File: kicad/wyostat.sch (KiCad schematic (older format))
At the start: 75 parts, among them J1 24 V AC IN, J13 USB_microAB, J16 5V_SEL, J2 OUT1, J3 OUT2, J4 OUT3, J5 I2C_ext1, Q1 BT136-600, Q2 BT136-600, Q3 BT136-600, U1 MOC3063M, U2 MOC3063M, U3 MOC3063M, U4 Wemos-Lolin, U5 MAX17502FATB+T

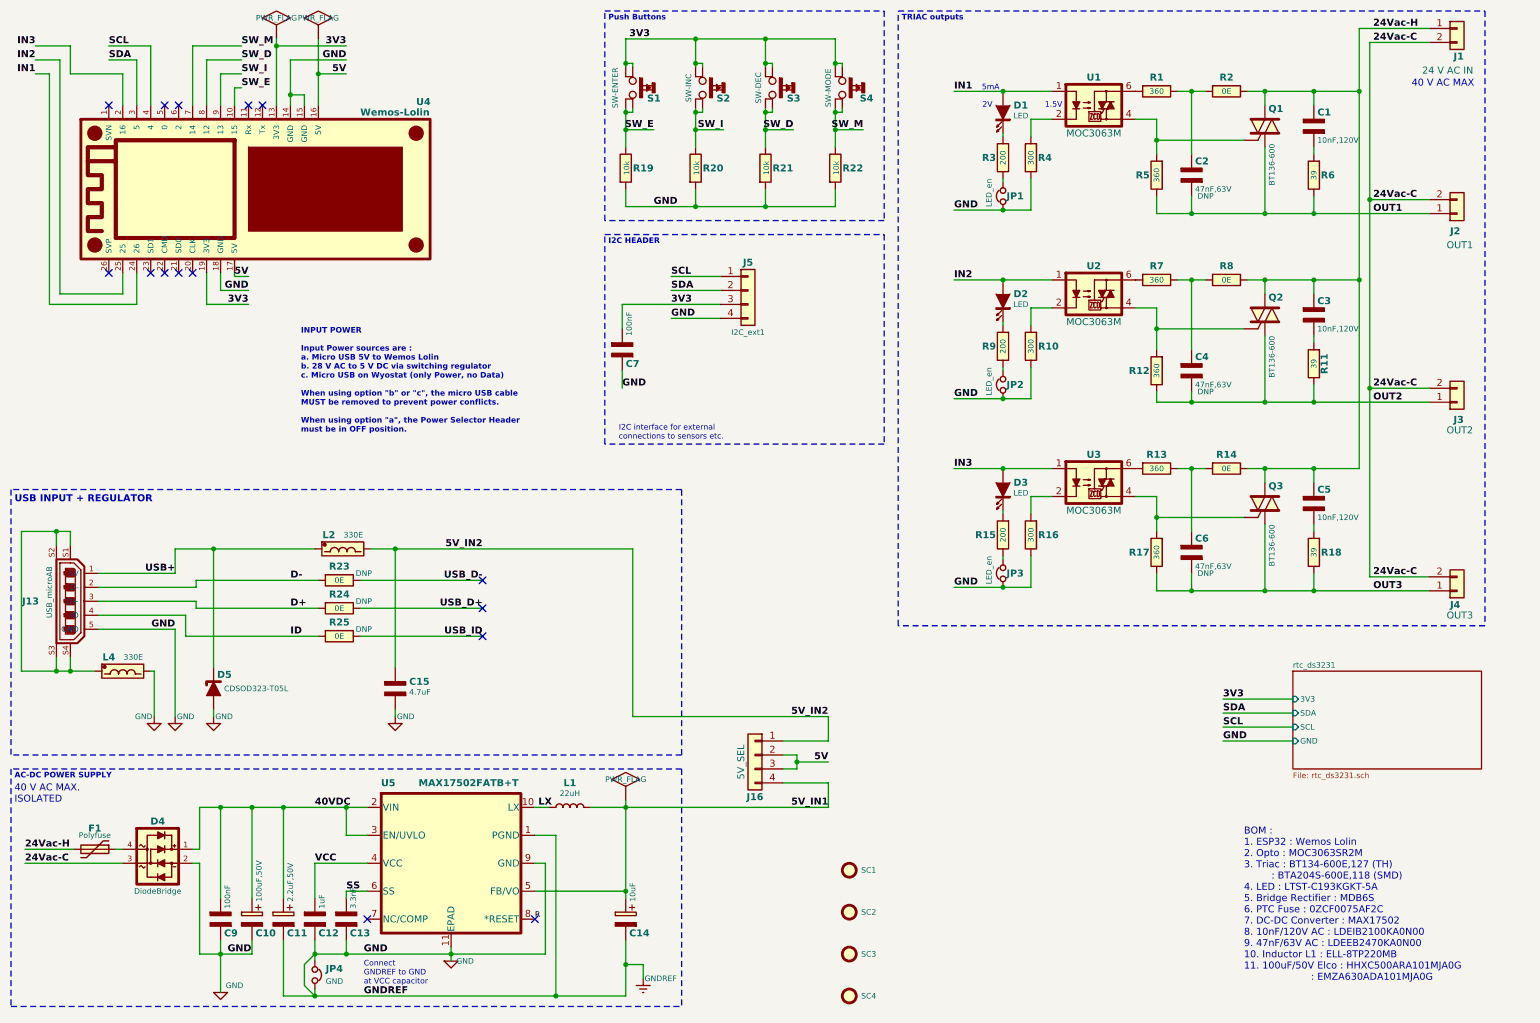
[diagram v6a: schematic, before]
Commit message: adding pads for spring contacts
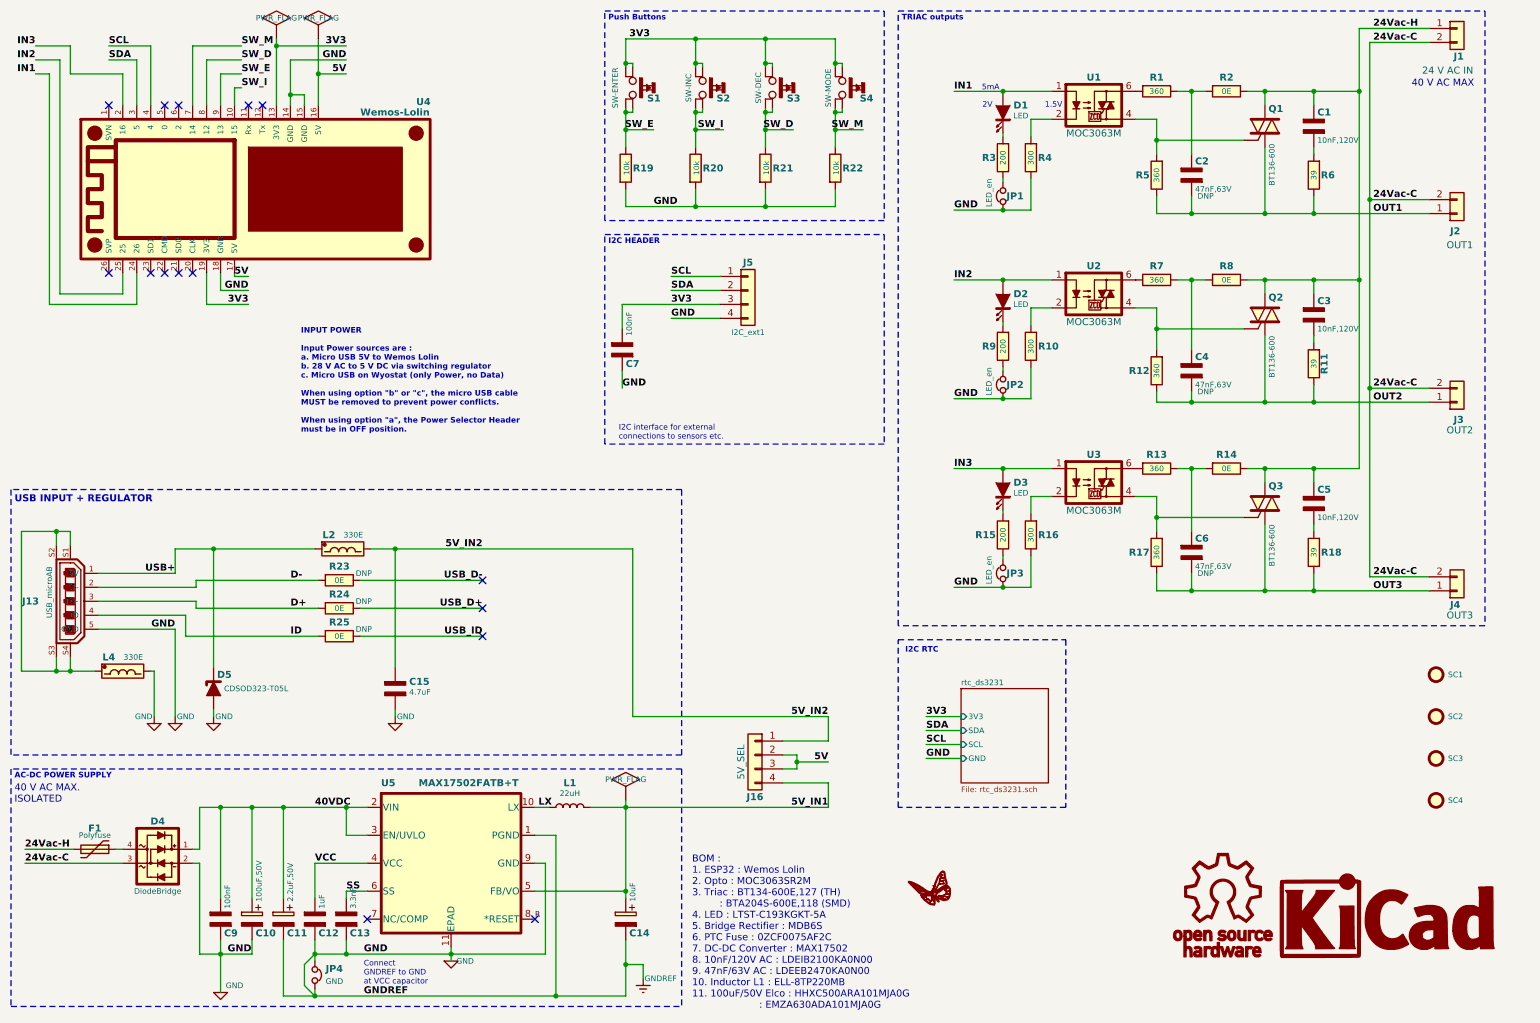
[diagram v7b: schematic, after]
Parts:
- added G1: LOGO_WL, wyostat_fp:Logo-WL3, symbol wyostat:LOGO_WL
- added G2: OSHW, wyostat_fp:OSHW_6mm, symbol wyostat:OSHW
- added G3: KiCad, wyostat_fp:KiCad-Logo2_6mm_SilkScreen, symbol wyostat:KiCad
- U1, U2, U3: footprint wyostat_fp:Optocoupler_6pin -> wyostat_fp:Optocoupler_6pin_smd
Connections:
- net SW_E: now also U4.9 (13); no longer U4.10 (15)
- net SW_I: now also U4.10 (15); no longer U4.9 (13)
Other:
- note added: "I2C RTC"
- moved on the sheet: SC1, SC2, SC3, SC4
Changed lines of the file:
@@
 Comment4 ""
 $EndDescr
-Text Notes 9400 7525 0    50   ~ 0
+Text Notes 5450 7725 0    50   ~ 0
 BOM :\n1. ESP32 : Wemos Lolin\n2. Opto : MOC3063SR2M\n3. Triac : BT134-600E,127 (TH)\n         : BTA204S-600E,118 (SMD)\n4. LED : LTST-C193KGKT-5A\n5. Bridge Rectifier : MDB6S\n6. PTC Fuse : 0ZCF0075AF2C\n7. DC-DC Converter : MAX17502\n8. 10nF/120V AC : LDEIB2100KA0N00\n9. 47nF/63V AC : LDEEB2470KA0N00\n10. Inductor L1 : ELL-8TP220MB\n11. 100uF/50V Elco : HHXC500ARA101MJA0G\n                      : EMZA630ADA101MJA0G
 $Comp
@@
 F 0 "U1" H 8325 1450 50  0000 C CNB
 F 1 "MOC3063M" H 8325 1050 50  0000 C CNN
-F 2 "wyostat_fp:Optocoupler_6pin" H 8125 1050 50  0001 L CIN
+F 2 "wyostat_fp:Optocoupler_6pin_smd" H 8125 1050 50  0001 L CIN
 F 3 "" H 8290 1250 50  0001 L CNN
 	1    8325 1250
@@
 F 0 "U2" H 8325 2800 50  0000 C CNB
 F 1 "MOC3063M" H 8325 2400 50  0000 C CNN
-F 2 "wyostat_fp:Optocoupler_6pin" H 8125 2400 50  0001 L CIN
+F 2 "wyostat_fp:Optocoupler_6pin_smd" H 8125 2400 50  0001 L CIN
 F 3 "" H 8290 2600 50  0001 L CNN
 	1    8325 2600
@@
 F 0 "U3" H 8325 4150 50  0000 C CNB
 F 1 "MOC3063M" H 8325 3750 50  0000 C CNN
-F 2 "wyostat_fp:Optocoupler_6pin" H 8125 3750 50  0001 L CIN
+F 2 "wyostat_fp:Optocoupler_6pin_smd" H 8125 3750 50  0001 L CIN
 F 3 "" H 8290 3950 50  0001 L CNN
 	1    8325 3950
@@
 Text Notes 6950 650  0    40   ~ 8
 TRIAC outputs
-Text Label 2225 1125 0    50   ~ 10
-SW_E
 Text Label 2225 1025 0    50   ~ 10
+SW_E
+Text Label 2225 1125 0    50   ~ 10
 SW_I
 Text Label 2225 925  0    50   ~ 10
@@
 L wyostat:SCREW SC1
 U 1 1 5AED1CEA
-P 6575 6725
-F 0 "SC1" H 6660 6725 40  0000 L CNN
-F 1 "SCREW" H 6575 6825 40  0001 C CNN
-F 2 "wyostat_fp:MountingHole_3.2mm_M3_Pad_Via" H 6575 6725 60  0001 C CNN
-F 3 "" H 6575 6725 60  0000 C CNN
-	1    6575 6725
+P 10775 5325
+F 0 "SC1" H 10860 5325 40  0000 L CNN
+F 1 "SCREW" H 10775 5425 40  0001 C CNN
+F 2 "wyostat_fp:MountingHole_3.2mm_M3_Pad_Via" H 10775 5325 60  0001 C CNN
+F 3 "" H 10775 5325 60  0000 C CNN
+	1    10775 5325
 	1    0    0    -1
 $EndComp
@@
 L wyostat:SCREW SC2
 U 1 1 5AED2014
-P 6575 7025
-F 0 "SC2" H 6660 7025 40  0000 L CNN
-F 1 "SCREW" H 6575 7125 40  0001 C CNN
-F 2 "wyostat_fp:MountingHole_3.2mm_M3_Pad_Via" H 6575 7025 60  0001 C CNN
-F 3 "" H 6575 7025 60  0000 C CNN
-	1    6575 7025
+P 10775 5625
+F 0 "SC2" H 10860 5625 40  0000 L CNN
+F 1 "SCREW" H 10775 5725 40  0001 C CNN
+F 2 "wyostat_fp:MountingHole_3.2mm_M3_Pad_Via" H 10775 5625 60  0001 C CNN
+F 3 "" H 10775 5625 60  0000 C CNN
+	1    10775 5625
 	1    0    0    -1
 $EndComp
@@
 L wyostat:SCREW SC3
 U 1 1 5AED2111
-P 6575 7325
-F 0 "SC3" H 6660 7325 40  0000 L CNN
-F 1 "SCREW" H 6575 7425 40  0001 C CNN
-F 2 "wyostat_fp:MountingHole_3.2mm_M3_Pad_Via" H 6575 7325 60  0001 C CNN
-F 3 "" H 6575 7325 60  0000 C CNN
-	1    6575 7325
+P 10775 5925
+F 0 "SC3" H 10860 5925 40  0000 L CNN
+F 1 "SCREW" H 10775 6025 40  0001 C CNN
+F 2 "wyostat_fp:MountingHole_3.2mm_M3_Pad_Via" H 10775 5925 60  0001 C CNN
+F 3 "" H 10775 5925 60  0000 C CNN
+	1    10775 5925
 	1    0    0    -1
 $EndComp
@@
 L wyostat:SCREW SC4
 U 1 1 5AED2331
-P 6575 7625
-F 0 "SC4" H 6660 7625 40  0000 L CNN
-F 1 "SCREW" H 6575 7725 40  0001 C CNN
-F 2 "wyostat_fp:MountingHole_3.2mm_M3_Pad_Via" H 6575 7625 60  0001 C CNN
-F 3 "" H 6575 7625 60  0000 C CNN
-	1    6575 7625
+P 10775 6225
+F 0 "SC4" H 10860 6225 40  0000 L CNN
+F 1 "SCREW" H 10775 6325 40  0001 C CNN
+F 2 "wyostat_fp:MountingHole_3.2mm_M3_Pad_Via" H 10775 6225 60  0001 C CNN
+F 3 "" H 10775 6225 60  0000 C CNN
+	1    10775 6225
 	1    0    0    -1
 $EndComp
@@
 	3325 4425 5025 4425
 $Sheet
-S 9750 5300 1350 700
+S 7375 5425 625  675
 U 5AE47A99
 F0 "rtc_ds3231" 40
 F1 "rtc_ds3231.sch" 40
-F2 "3V3" I L 9750 5500 40
-F3 "GND" I L 9750 5800 40
-F4 "SDA" I L 9750 5600 40
-F5 "SCL" I L 9750 5700 40
+F2 "3V3" I L 7375 5625 40
+F3 "GND" I L 7375 5925 40
+F4 "SDA" I L 7375 5725 40
+F5 "SCL" I L 7375 5825 40
 $EndSheet
 Wire Wire Line
-	9750 5500 9250 5500
+	7375 5625 7125 5625
 Wire Wire Line
-	9250 5600 9750 5600
+	7125 5725 7375 5725
 Wire Wire Line
-	9750 5700 9250 5700
+	7375 5825 7125 5825
 Wire Wire Line
-	9250 5800 9750 5800
-Text Label 9250 5800 0    50   ~ 10
+	7125 5925 7375 5925
+Text Label 7125 5925 0    50   ~ 10
 GND
-Text Label 9250 5500 0    50   ~ 10
+Text Label 7125 5625 0    50   ~ 10
 3V3
-Text Label 9250 5700 0    50   ~ 10
+Text Label 7125 5825 0    50   ~ 10
 SCL
-Text Label 9250 5600 0    50   ~ 10
+Text Label 7125 5725 0    50   ~ 10
 SDA
+Wire Notes Line
+	8125 5075 8125 6275
+Wire Notes Line
+	8125 6275 6925 6275
+Wire Notes Line
+	6925 6275 6925 5075
+Wire Notes Line
+	6925 5075 8125 5075
+Text Notes 6975 5175 0    40   ~ 8
+I2C RTC
+$Comp
+L wyostat:KiCad G3
+U 1 1 5AC0C01C
+P 10425 7050
+F 0 "G3" H 10425 6782 60  0001 C CNN
+F 1 "KiCad" H 10425 7318 60  0001 C CNN
+F 2 "wyostat_fp:KiCad-Logo2_6mm_SilkScreen" H 10425 7050 60  0001 C CNN
+F 3 "" H 10425 7050 60  0001 C CNN
+F 4 "Value" H 10425 7050 50  0001 C CNN "manf#"
+	1    10425 7050
+	1    0    0    -1
+$EndComp
+$Comp
+L wyostat:LOGO_WL G1
+U 1 1 5AC0C12D
+P 7175 6875
+F 0 "G1" H 7175 6739 60  0001 C CNN
+F 1 "LOGO_WL" H 7175 7011 60  0001 C CNN
+F 2 "wyostat_fp:Logo-WL3" H 7175 6875 60  0001 C CNN
+F 3 "" H 7175 6875 60  0001 C CNN
+F 4 "Value" H 7175 6875 50  0001 C CNN "manf#"
+	1    7175 6875
+	1    0    0    -1
+$EndComp
+$Comp
+L wyostat:OSHW G2
+U 1 1 5AC0C24A
+P 9250 6975
+F 0 "G2" H 9250 6925 40  0001 C CNN
+F 1 "OSHW" H 9250 7075 40  0001 C CNN
+F 2 "wyostat_fp:OSHW_6mm" H 9250 6975 60  0001 C CNN
+F 3 "" H 9250 6975 60  0000 C CNN
+F 4 "Value" H 9250 6975 50  0001 C CNN "manf#"
+	1    9250 6975
+	1    0    0    -1
+$EndComp
 $EndSCHEMATC
